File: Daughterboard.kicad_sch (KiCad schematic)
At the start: 61 parts, among them U1 SI8271GB-IS, U2 SI8271GB-IS, U3 GS61004B, U4 IES0105S09, U5 GS61004B, U6 IES0105S09

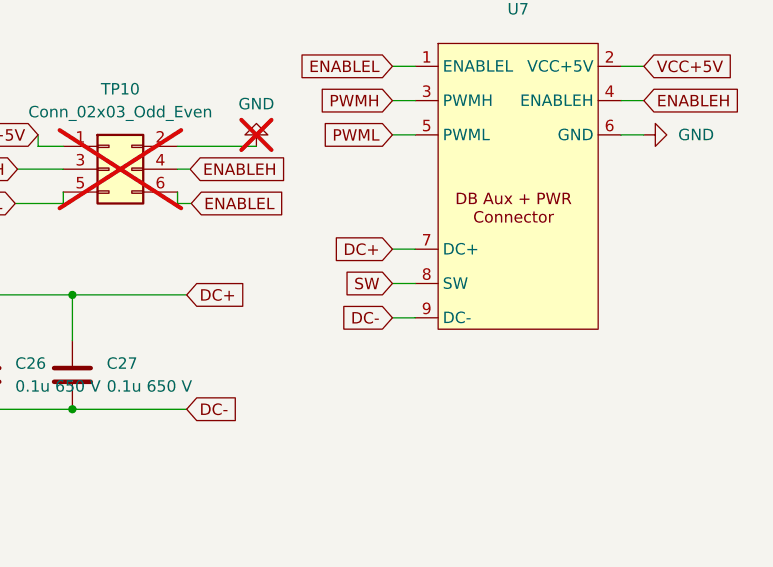
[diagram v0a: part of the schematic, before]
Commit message: start layout design, component placement
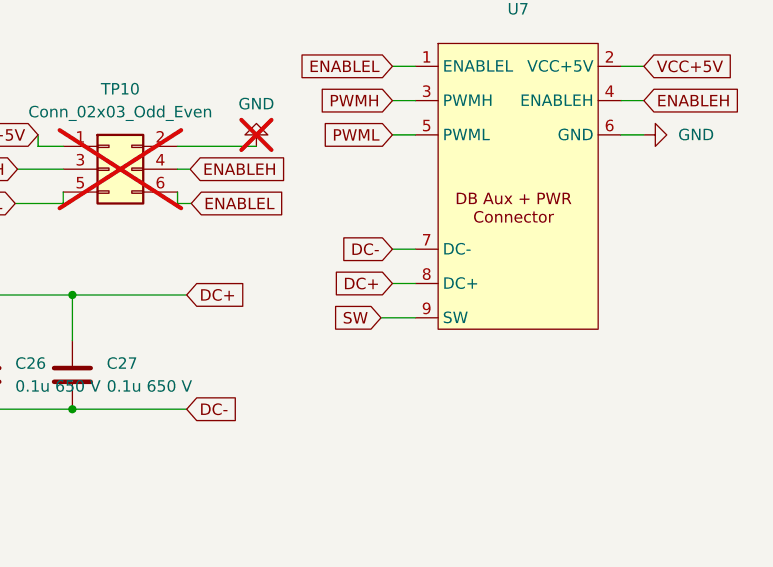
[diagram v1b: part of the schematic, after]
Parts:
- U7: symbol New_Library_0:DB_to_MB_conn -> DB_to_MB_conn:DB_to_MB_conn
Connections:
- net DC+: now also U7.8 (DC+); no longer U7.7 (DC+)
- net DC-: now also U7.7 (DC-); no longer U7.9 (DC-)
- net SW: now also U7.9 (SW); no longer U7.8 (SW)
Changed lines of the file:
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@@
 	(wire
 		(pts
-			(xy 363.22 48.26) (xy 365.76 48.26)
-		)
-		(stroke
-			(width 0)
-			(type default)
-		)
-	)
-	(wire
-		(pts
 			(xy 219.71 185.42) (xy 219.71 187.96)
 		)
@@
 	(wire
 		(pts
+			(xy 361.95 48.26) (xy 365.76 48.26)
+		)
+		(stroke
+			(width 0)
+			(type default)
+		)
+	)
+	(wire
+		(pts
 			(xy 78.74 29.21) (xy 105.41 29.21)
 		)
@@
 	(wire
 		(pts
-			(xy 363.22 44.45) (xy 365.76 44.45)
-		)
-		(stroke
-			(width 0)
-			(type default)
-		)
-	)
-	(wire
-		(pts
 			(xy 58.42 29.21) (xy 78.74 29.21)
 		)
@@
 	(wire
 		(pts
+			(xy 363.22 44.45) (xy 365.76 44.45)
+		)
+		(stroke
+			(width 0)
+			(type default)
+		)
+	)
+	(wire
+		(pts
 			(xy 194.31 102.87) (xy 214.63 102.87)
 		)
@@
 	(wire
 		(pts
-			(xy 363.22 40.64) (xy 365.76 40.64)
-		)
-		(stroke
-			(width 0)
-			(type default)
-		)
-	)
-	(wire
-		(pts
 			(xy 105.41 243.84) (xy 105.41 247.65)
 		)
@@
 	(wire
 		(pts
+			(xy 363.22 40.64) (xy 365.76 40.64)
+		)
+		(stroke
+			(width 0)
+			(type default)
+		)
+	)
+	(wire
+		(pts
 			(xy 190.5 185.42) (xy 179.07 185.42)
 		)
@@
 	(global_label "DC+"
 		(shape input)
-		(at 363.22 40.64 180)
+		(at 363.22 44.45 180)
 		(fields_autoplaced yes)
 		(effects
@@
 		)
 		(property "Intersheetrefs" "${INTERSHEET_REFS}"
-			(at 356.1224 40.64 0)
+			(at 356.1224 44.45 0)
 			(effects
 				(font
@@
 	(global_label "SW"
 		(shape input)
-		(at 363.22 44.45 180)
+		(at 361.95 48.26 180)
 		(fields_autoplaced yes)
 		(effects
@@
 		)
 		(property "Intersheetrefs" "${INTERSHEET_REFS}"
-			(at 357.5739 44.45 0)
+			(at 356.3039 48.26 0)
 			(effects
 				(font
@@
 	(global_label "DC-"
 		(shape input)
-		(at 363.22 48.26 180)
+		(at 363.22 40.64 180)
 		(fields_autoplaced yes)
 		(effects
@@
 		)
 		(property "Intersheetrefs" "${INTERSHEET_REFS}"
-			(at 356.1224 48.26 0)
+			(at 356.1224 40.64 0)
 			(effects
 				(font
@@
 	)
 	(symbol
-		(lib_id "New_Library_0:DB_to_MB_conn")
+		(lib_id "DB_to_MB_conn:DB_to_MB_conn")
 		(at 377.19 33.02 0)
 		(unit 1)

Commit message: initial version for commenting
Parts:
- TP13, TP14, TP15, TP16, TP17, TP18, TP19: footprint TestPoint:TestPoint_Pad_D2.0mm -> TestPoint:TestPoint_THTPad_D1.0mm_Drill0.5mm
- U3, U5: footprint GS61004B:GS61004B -> GS61004B:GS6XXX4B
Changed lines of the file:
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@@
 			)
 		)
-		(property "Footprint" "TestPoint:TestPoint_Pad_D2.0mm"
+		(property "Footprint" "TestPoint:TestPoint_THTPad_D1.0mm_Drill0.5mm"
 			(at 341.63 125.73 0)
 			(effects
@@
 			)
 		)
-		(property "Footprint" "TestPoint:TestPoint_Pad_D2.0mm"
+		(property "Footprint" "TestPoint:TestPoint_THTPad_D1.0mm_Drill0.5mm"
 			(at 341.503 107.823 0)
 			(effects
@@
 			)
 		)
-		(property "Footprint" "GS61004B:GS61004B"
+		(property "Footprint" "GS61004B:GS6XXX4B"
 			(at 232.41 231.14 0)
 			(effects
@@
 			)
 		)
-		(property "Footprint" "TestPoint:TestPoint_Pad_D2.0mm"
+		(property "Footprint" "TestPoint:TestPoint_THTPad_D1.0mm_Drill0.5mm"
 			(at 355.6 125.73 0)
 			(effects
@@
 			)
 		)
-		(property "Footprint" "TestPoint:TestPoint_Pad_D2.0mm"
+		(property "Footprint" "TestPoint:TestPoint_THTPad_D1.0mm_Drill0.5mm"
 			(at 325.12 125.73 0)
 			(effects
@@
 			)
 		)
-		(property "Footprint" "TestPoint:TestPoint_Pad_D2.0mm"
+		(property "Footprint" "TestPoint:TestPoint_THTPad_D1.0mm_Drill0.5mm"
 			(at 324.993 107.823 0)
 			(effects
@@
 			)
 		)
-		(property "Footprint" "TestPoint:TestPoint_Pad_D2.0mm"
+		(property "Footprint" "TestPoint:TestPoint_THTPad_D1.0mm_Drill0.5mm"
 			(at 314.96 125.73 0)
 			(effects
@@
 			)
 		)
-		(property "Footprint" "TestPoint:TestPoint_Pad_D2.0mm"
+		(property "Footprint" "TestPoint:TestPoint_THTPad_D1.0mm_Drill0.5mm"
 			(at 355.473 107.823 0)
 			(effects
@@
 			)
 		)
-		(property "Footprint" "GS61004B:GS61004B"
+		(property "Footprint" "GS61004B:GS6XXX4B"
 			(at 232.41 93.98 0)
 			(effects

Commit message: fixed after comments
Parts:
- TP10: footprint (none) -> 3x2_connector:CON6_2X3_TU_TSW_SAI; now fitted
- U1, U2: footprint Package_SO:SOIC-8-1EP_3.9x4.9mm_P1.27mm_EP2.29x3mm -> Package_SO:SOIC-8_3.9x4.9mm_P1.27mm
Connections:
- net ENABLEL: now also TP10.1 (Pin_1); no longer TP10.6 (Pin_6)
- net GND: now also TP10.6 (Pin_6); no longer TP10.2 (Pin_2)
- net VCC+5V: now also TP10.2 (Pin_2); no longer TP10.1 (Pin_1)
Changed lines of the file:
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@@
 	(wire
 		(pts
-			(xy 124.46 106.68) (xy 105.41 106.68)
+			(xy 339.09 36.83) (xy 340.36 36.83)
 		)
 		(stroke
@@
 	(wire
 		(pts
-			(xy 323.85 27.94) (xy 323.85 29.21)
+			(xy 124.46 106.68) (xy 105.41 106.68)
 		)
 		(stroke
@@
 	(wire
 		(pts
+			(xy 321.31 34.29) (xy 321.31 35.56)
+		)
+		(stroke
+			(width 0)
+			(type default)
+		)
+	)
+	(wire
+		(pts
 			(xy 124.46 101.6) (xy 124.46 100.33)
 		)
@@
 	(wire
 		(pts
+			(xy 326.644 29.21) (xy 323.85 29.21)
+		)
+		(stroke
+			(width 0)
+			(type default)
+		)
+	)
+	(wire
+		(pts
 			(xy 273.05 45.72) (xy 273.05 50.8)
 		)
@@
 	(wire
 		(pts
-			(xy 339.344 35.56) (xy 339.344 34.29)
+			(xy 339.09 33.02) (xy 341.63 33.02)
 		)
 		(stroke
@@
 	(wire
 		(pts
+			(xy 339.09 34.29) (xy 339.344 34.29)
+		)
+		(stroke
+			(width 0)
+			(type default)
+		)
+	)
+	(wire
+		(pts
 			(xy 220.98 246.38) (xy 240.03 246.38)
 		)
@@
 	(wire
 		(pts
-			(xy 348.107 29.21) (xy 339.344 29.21)
-		)
-		(stroke
-			(width 0)
-			(type default)
-		)
-	)
-	(wire
-		(pts
 			(xy 176.53 24.13) (xy 176.53 26.67)
 		)
@@
 	(wire
 		(pts
+			(xy 339.09 33.02) (xy 339.09 31.75)
+		)
+		(stroke
+			(width 0)
+			(type default)
+		)
+	)
+	(wire
+		(pts
 			(xy 158.75 240.03) (xy 158.75 237.49)
 		)
@@
 	(wire
 		(pts
-			(xy 323.85 29.21) (xy 326.644 29.21)
-		)
-		(stroke
-			(width 0)
-			(type default)
-		)
-	)
-	(wire
-		(pts
 			(xy 391.16 24.13) (xy 388.62 24.13)
 		)
@@
 	(wire
 		(pts
-			(xy 326.644 35.56) (xy 326.644 34.29)
-		)
-		(stroke
-			(width 0)
-			(type default)
-		)
-	)
-	(wire
-		(pts
 			(xy 319.913 107.823) (xy 319.913 110.363)
 		)
@@
 	(wire
 		(pts
+			(xy 339.09 36.83) (xy 339.09 34.29)
+		)
+		(stroke
+			(width 0)
+			(type default)
+		)
+	)
+	(wire
+		(pts
 			(xy 190.5 185.42) (xy 179.07 185.42)
 		)
@@
 	(wire
 		(pts
-			(xy 321.564 31.75) (xy 326.644 31.75)
+			(xy 321.31 31.75) (xy 326.644 31.75)
 		)
 		(stroke
@@
 	(wire
 		(pts
+			(xy 339.09 31.75) (xy 339.344 31.75)
+		)
+		(stroke
+			(width 0)
+			(type default)
+		)
+	)
+	(wire
+		(pts
 			(xy 48.26 26.67) (xy 48.26 27.94)
 		)
@@
 	(wire
 		(pts
+			(xy 326.644 34.29) (xy 321.31 34.29)
+		)
+		(stroke
+			(width 0)
+			(type default)
+		)
+	)
+	(wire
+		(pts
 			(xy 82.55 238.76) (xy 124.46 238.76)
 		)
@@
 	(wire
 		(pts
-			(xy 340.868 35.56) (xy 339.344 35.56)
-		)
-		(stroke
-			(width 0)
-			(type default)
-		)
-	)
-	(wire
-		(pts
 			(xy 205.74 46.99) (xy 205.74 49.53)
 		)
@@
 	(wire
 		(pts
-			(xy 294.64 58.42) (xy 306.07 58.42)
+			(xy 339.344 29.21) (xy 341.63 29.21)
 		)
 		(stroke
@@
 	(wire
 		(pts
-			(xy 327.66 45.72) (xy 327.66 50.8)
+			(xy 294.64 58.42) (xy 306.07 58.42)
 		)
 		(stroke
@@
 	(wire
 		(pts
-			(xy 363.22 24.13) (xy 365.76 24.13)
+			(xy 327.66 45.72) (xy 327.66 50.8)
 		)
 		(stroke
@@
 	(wire
 		(pts
-			(xy 186.69 203.2) (xy 186.69 207.01)
+			(xy 363.22 24.13) (xy 365.76 24.13)
 		)
 		(stroke
@@
 	(wire
 		(pts
-			(xy 176.53 34.29) (xy 176.53 49.53)
+			(xy 186.69 203.2) (xy 186.69 207.01)
 		)
 		(stroke
@@
 	(wire
 		(pts
-			(xy 273.05 45.72) (xy 284.48 45.72)
+			(xy 176.53 34.29) (xy 176.53 49.53)
 		)
 		(stroke
@@
 	(wire
 		(pts
-			(xy 321.31 35.56) (xy 326.644 35.56)
+			(xy 273.05 45.72) (xy 284.48 45.72)
 		)
 		(stroke
@@
 	(wire
 		(pts
-			(xy 339.344 31.75) (xy 340.741 31.75)
-		)
-		(stroke
-			(width 0)
-			(type default)
-		)
-	)
-	(wire
-		(pts
 			(xy 82.55 101.6) (xy 124.46 101.6)
 		)
@@
 	(global_label "ENABLEH"
 		(shape input)
-		(at 340.741 31.75 0)
+		(at 341.63 33.02 0)
 		(fields_autoplaced yes)
 		(effects
@@
 		)
 		(property "Intersheetrefs" "${INTERSHEET_REFS}"
-			(at 352.0719 31.75 0)
+			(at 352.9609 33.02 0)
 			(effects
 				(font
@@
 	(global_label "PWMH"
 		(shape input)
-		(at 321.564 31.75 180)
+		(at 321.31 31.75 180)
 		(fields_autoplaced yes)
 		(effects
@@
 		)
 		(property "Intersheetrefs" "${INTERSHEET_REFS}"
-			(at 313.0755 31.75 0)
+			(at 312.8215 31.75 0)
 			(effects
 				(font
@@
 	(global_label "ENABLEL"
 		(shape input)
-		(at 340.868 35.56 0)
+		(at 323.85 29.21 180)
 		(fields_autoplaced yes)
 		(effects
@@
 				(size 1.27 1.27)
 			)
-			(justify left)
+			(justify right)
 		)
 		(property "Intersheetrefs" "${INTERSHEET_REFS}"
-			(at 351.8965 35.56 0)
+			(at 312.8215 29.21 0)
 			(effects
 				(font
 					(size 1.27 1.27)
 				)
-				(justify left)
+				(justify right)
 				(hide yes)
 			)
@@
 	(global_label "VCC+5V"
 		(shape input)
-		(at 323.85 27.94 180)
+		(at 341.63 29.21 0)
 		(fields_autoplaced yes)
 		(effects
@@
 				(size 1.27 1.27)
 			)
-			(justify right)
+			(justify left)
 		)
 		(property "Intersheetrefs" "${INTERSHEET_REFS}"
-			(at 313.3657 27.94 0)
+			(at 352.1143 29.21 0)
 			(effects
 				(font
 					(size 1.27 1.27)
 				)
-				(justify right)
+				(justify left)
 				(hide yes)
 			)
@@
 	(symbol
 		(lib_id "power:GND")
-		(at 348.107 29.21 180)
+		(at 340.36 36.83 0)
 		(unit 1)
 		(exclude_from_sim no)
 		(in_bom yes)
 		(on_board yes)
-		(dnp yes)
+		(dnp no)
 		(fields_autoplaced yes)
 		(property "Reference" "#PWR014"
-			(at 348.107 22.86 0)
+			(at 340.36 43.18 0)
 			(effects
 				(font
@@
 		)
 		(property "Value" "GND"
-			(at 348.107 24.511 0)
+			(at 340.36 41.91 0)
 			(effects
 				(font
@@
 		)
 		(property "Footprint" ""
-			(at 348.107 29.21 0)
+			(at 340.36 36.83 0)
 			(effects
 				(font
@@
 		)
 		(property "Datasheet" ""
-			(at 348.107 29.21 0)
+			(at 340.36 36.83 0)
 			(effects
 				(font
@@
 		)
 		(property "Description" ""
-			(at 348.107 29.21 0)
+			(at 340.36 36.83 0)
 			(effects
 				(font
@@
 			)
 		)
-		(property "Footprint" "Package_SO:SOIC-8-1EP_3.9x4.9mm_P1.27mm_EP2.29x3mm"
+		(property "Footprint" "Package_SO:SOIC-8_3.9x4.9mm_P1.27mm"
 			(at 149.86 242.57 0)
 			(effects
@@
 		(in_bom yes)
 		(on_board yes)
-		(dnp yes)
+		(dnp no)
 		(fields_autoplaced yes)
 		(property "Reference" "TP10"
@@
 			)
 		)
-		(property "Footprint" ""
+		(property "Footprint" "3x2_connector:CON6_2X3_TU_TSW_SAI"
 			(at 331.724 31.75 0)
 			(effects
@@
 			)
 		)
-		(property "Footprint" "Package_SO:SOIC-8-1EP_3.9x4.9mm_P1.27mm_EP2.29x3mm"
+		(property "Footprint" "Package_SO:SOIC-8_3.9x4.9mm_P1.27mm"
 			(at 149.86 105.41 0)
 			(effects

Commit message: gerbers, drill files and pick-and-place added, deleted unneccessary items from BOM
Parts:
- D1, D2, R12, R14, R6, R7: JLCPCB BOM (none) -> 1
- TP10, TP13, TP14, TP15, TP16, TP17, TP18, TP19, U1, U2, U3, U4, U5, U6, U7: JLCPCB BOM (none) -> 0
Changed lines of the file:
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@@
 			)
 		)
-		(property "JLCPCB BOM" ""
+		(property "JLCPCB BOM" "0"
 			(at 336.55 125.73 0)
 			(effects
@@
 			)
 		)
-		(property "JLCPCB BOM" ""
+		(property "JLCPCB BOM" "0"
 			(at 336.423 107.823 0)
 			(effects
@@
 			)
 		)
-		(property "JLCPCB BOM" ""
+		(property "JLCPCB BOM" "0"
 			(at 232.41 231.14 0)
 			(effects
@@
 			)
 		)
-		(property "JLCPCB BOM" ""
+		(property "JLCPCB BOM" "0"
 			(at 350.52 125.73 0)
 			(effects
@@
 			)
 		)
-		(property "JLCPCB BOM" ""
+		(property "JLCPCB BOM" "0"
 			(at 106.68 27.94 0)
 			(effects
@@
 			)
 		)
-		(property "JLCPCB BOM" ""
+		(property "JLCPCB BOM" "0"
 			(at 149.86 242.57 0)
 			(effects
@@
 			)
 		)
-		(property "JLCPCB BOM" ""
+		(property "JLCPCB BOM" "0"
 			(at 320.04 125.73 0)
 			(effects
@@
 			)
 		)
-		(property "JLCPCB BOM" ""
+		(property "JLCPCB BOM" "0"
 			(at 120.65 163.83 0)
 			(effects
@@
 			)
 		)
-		(property "JLCPCB BOM" ""
+		(property "JLCPCB BOM" "1"
 			(at 220.98 101.6 0)
 			(effects
@@
 			)
 		)
-		(property "JLCPCB BOM" ""
+		(property "JLCPCB BOM" "0"
 			(at 319.913 107.823 0)
 			(effects
@@
 			)
 		)
-		(property "JLCPCB BOM" ""
+		(property "JLCPCB BOM" "1"
 			(at 220.98 238.76 0)
 			(effects
@@
 			)
 		)
-		(property "JLCPCB BOM" ""
+		(property "JLCPCB BOM" "1"
 			(at 207.01 165.1 0)
 			(effects
@@
 			)
 		)
-		(property "JLCPCB BOM" ""
+		(property "JLCPCB BOM" "1"
 			(at 207.01 175.26 0)
 			(effects
@@
 			)
 		)
-		(property "JLCPCB BOM" ""
+		(property "JLCPCB BOM" "0"
 			(at 377.19 33.02 0)
 			(effects
@@
 			)
 		)
-		(property "JLCPCB BOM" ""
+		(property "JLCPCB BOM" "1"
 			(at 193.04 29.21 0)
 			(effects
@@
 			)
 		)
-		(property "JLCPCB BOM" ""
+		(property "JLCPCB BOM" "1"
 			(at 193.04 39.37 0)
 			(effects
@@
 			)
 		)
-		(property "JLCPCB BOM" ""
+		(property "JLCPCB BOM" "0"
 			(at 331.724 31.75 0)
 			(effects
@@
 			)
 		)
-		(property "JLCPCB BOM" ""
+		(property "JLCPCB BOM" "0"
 			(at 309.88 125.73 0)
 			(effects
@@
 			)
 		)
-		(property "JLCPCB BOM" ""
+		(property "JLCPCB BOM" "0"
 			(at 350.393 107.823 0)
 			(effects
@@
 			)
 		)
-		(property "JLCPCB BOM" ""
+		(property "JLCPCB BOM" "0"
 			(at 149.86 105.41 0)
 			(effects
@@
 			)
 		)
-		(property "JLCPCB BOM" ""
+		(property "JLCPCB BOM" "0"
 			(at 232.41 93.98 0)
 			(effects
